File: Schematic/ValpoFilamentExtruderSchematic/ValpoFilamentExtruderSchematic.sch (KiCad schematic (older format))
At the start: 1 part

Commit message: Schematic Started
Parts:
- added A?: A000067, ARDUINO_A000067, symbol ArduinoMega2560:A000067
- added M? (x2): Motor_Servo, symbol Motor:Motor_Servo
- added M?: Fan_3pin, symbol Motor:Fan_3pin
- added R?: 10k, symbol Device:R
- added TH? (x2): JTypeThermocouple, symbol Sensor_Temperature:PT100
- added U?: HeatingElement, symbol FilamentRecycler09:HeatingElement
- added U?: 120ACV_24VDC, symbol FilamentRecycler09:120ACV_24VDC
- added U?: A1101ELHL, Package_TO_SOT_SMD:SOT-23, symbol Sensor_Magnetic:A1101ELHL
- added U?: 24V_5V, symbol FilamentRecycler09:24V_5V
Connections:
- new net: U?.2 (GND), U?.4 (-V)
- new net: R?.2, U?.2 (VOUT)
- new net +24V: U?.3 (+V), U?.3 (Vin)
- new net +5V: R?.1, U?.1 (VCC), U?.Vout (6)
- new net GND: U?.3 (GND)
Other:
- moved on the sheet: M?
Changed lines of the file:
@@
 L Motor:Motor_DC M?
 U 1 1 5F8662F0
-P 1750 1750
-F 0 "M?" H 1908 1746 50  0000 L CNN
-F 1 "Motor_DC" H 1908 1655 50  0000 L CNN
-F 2 "" H 1750 1660 50  0001 C CNN
-F 3 "~" H 1750 1660 50  0001 C CNN
-	1    1750 1750
-	1    0    0    -1
-$EndComp
+P 1250 2700
+F 0 "M?" H 1408 2696 50  0000 L CNN
+F 1 "Motor_DC" H 1408 2605 50  0000 L CNN
+F 2 "" H 1250 2610 50  0001 C CNN
+F 3 "~" H 1250 2610 50  0001 C CNN
+	1    1250 2700
+	1    0    0    -1
+$EndComp
+$Comp
+L ArduinoMega2560:A000067 A?
+U 1 1 5F887C03
+P 6850 3550
+F 0 "A?" H 6850 6117 50  0000 C CNN
+F 1 "A000067" H 6850 6026 50  0000 C CNN
+F 2 "ARDUINO_A000067" H 6850 3550 50  0001 L BNN
+F 3 "Unavailable" H 6850 3550 50  0001 L BNN
+F 4 "None" H 6850 3550 50  0001 L BNN "Field4"
+F 5 "Dev.kit: Arduino; SPI, TWI, UART; ICSP, USB B, pin strips, supply" H 6850 3550 50  0001 L BNN "Field5"
+F 6 "None" H 6850 3550 50  0001 L BNN "Field6"
+F 7 "ARDUINO MEGA2560 REV3 - RETAIL" H 6850 3550 50  0001 L BNN "Field7"
+F 8 "Arduino" H 6850 3550 50  0001 L BNN "Field8"
+	1    6850 3550
+	1    0    0    -1
+$EndComp
+$Comp
+L Sensor_Temperature:PT100 TH?
+U 1 1 5F890441
+P 2200 1600
+F 0 "TH?" H 2298 1646 50  0000 L CNN
+F 1 "JTypeThermocouple" H 2298 1555 50  0000 L CNN
+F 2 "" H 2200 1650 50  0001 C CNN
+F 3 "https://www.heraeus.com/media/media/group/doc_group/products_1/hst/sot_to/de_15/to_92_d.pdf" H 2200 1650 50  0001 C CNN
+	1    2200 1600
+	1    0    0    -1
+$EndComp
+$Comp
+L Sensor_Temperature:PT100 TH?
+U 1 1 5F891ED8
+P 1100 1600
+F 0 "TH?" H 1198 1646 50  0000 L CNN
+F 1 "JTypeThermocouple" H 1198 1555 50  0000 L CNN
+F 2 "" H 1100 1650 50  0001 C CNN
+F 3 "https://www.heraeus.com/media/media/group/doc_group/products_1/hst/sot_to/de_15/to_92_d.pdf" H 1100 1650 50  0001 C CNN
+	1    1100 1600
+	1    0    0    -1
+$EndComp
+$Comp
+L FilamentRecycler09:HeatingElement U?
+U 1 1 5F893064
+P 2800 900
+F 0 "U?" H 3042 1125 50  0000 C CNN
+F 1 "HeatingElement" H 3042 1034 50  0000 C CNN
+F 2 "" H 2800 1000 50  0001 C CNN
+F 3 "" H 2800 1000 50  0001 C CNN
+	1    2800 900
+	1    0    0    -1
+$EndComp
+$Comp
+L Motor:Motor_Servo M?
+U 1 1 5F8966D7
+P 4800 2100
+F 0 "M?" H 5132 2165 50  0000 L CNN
+F 1 "Motor_Servo" H 5132 2074 50  0000 L CNN
+F 2 "" H 4800 1910 50  0001 C CNN
+F 3 "http://forums.parallax.com/uploads/attachments/46831/74481.png" H 4800 1910 50  0001 C CNN
+	1    4800 2100
+	1    0    0    -1
+$EndComp
+$Comp
+L Motor:Motor_Servo M?
+U 1 1 5F88F163
+P 4800 2500
+F 0 "M?" H 5132 2565 50  0000 L CNN
+F 1 "Motor_Servo" H 5132 2474 50  0000 L CNN
+F 2 "" H 4800 2310 50  0001 C CNN
+F 3 "http://forums.parallax.com/uploads/attachments/46831/74481.png" H 4800 2310 50  0001 C CNN
+	1    4800 2500
+	1    0    0    -1
+$EndComp
+$Comp
+L FilamentRecycler09:120ACV_24VDC U?
+U 1 1 5F8A2677
+P 1650 4050
+F 0 "U?" H 1700 4615 50  0000 C CNN
+F 1 "120ACV_24VDC" H 1700 4524 50  0000 C CNN
+F 2 "" H 1650 4600 50  0001 C CNN
+F 3 "" H 1650 4600 50  0001 C CNN
+	1    1650 4050
+	1    0    0    -1
+$EndComp
+$Comp
+L FilamentRecycler09:24V_5V U?
+U 1 1 5F8A3A69
+P 3150 4000
+F 0 "U?" H 3175 4415 50  0000 C CNN
+F 1 "24V_5V" H 3175 4324 50  0000 C CNN
+F 2 "" H 3150 4250 50  0001 C CNN
+F 3 "" H 3150 4250 50  0001 C CNN
+	1    3150 4000
+	1    0    0    -1
+$EndComp
+Wire Wire Line
+	2100 3950 2150 3950
+Wire Wire Line
+	2500 3950 2500 4150
+Wire Wire Line
+	2500 4150 2850 4150
+Wire Wire Line
+	2850 4000 2250 4000
+Wire Wire Line
+	2250 4000 2250 4050
+Wire Wire Line
+	2250 4050 2100 4050
+$Comp
+L Motor:Fan_3pin M?
+U 1 1 5F8A2653
+P 4100 5100
+F 0 "M?" H 4258 5096 50  0000 L CNN
+F 1 "Fan_3pin" H 4258 5005 50  0000 L CNN
+F 2 "" H 4100 5010 50  0001 C CNN
+F 3 "http://www.hardwarecanucks.com/forum/attachments/new-builds/16287d1330775095-help-chassis-power-fan-connectors-motherboard-asus_p8z68.jpg" H 4100 5010 50  0001 C CNN
+	1    4100 5100
+	1    0    0    -1
+$EndComp
+$Comp
+L Sensor_Magnetic:A1101ELHL U?
+U 1 1 5F8A36D5
+P 1750 5400
+F 0 "U?" H 1520 5446 50  0000 R CNN
+F 1 "A1101ELHL" H 1520 5355 50  0000 R CNN
+F 2 "Package_TO_SOT_SMD:SOT-23" H 1750 5050 50  0001 L CIN
+F 3 "http://www.allegromicro.com/en/Products/Part_Numbers/1101/1101.pdf" H 1750 6050 50  0001 C CNN
+	1    1750 5400
+	1    0    0    -1
+$EndComp
+$Comp
+L Device:R R?
+U 1 1 5F8A3F4C
+P 2450 5400
+F 0 "R?" H 2520 5446 50  0000 L CNN
+F 1 "10k" H 2520 5355 50  0000 L CNN
+F 2 "" V 2380 5400 50  0001 C CNN
+F 3 "~" H 2450 5400 50  0001 C CNN
+	1    2450 5400
+	1    0    0    -1
+$EndComp
+Wire Wire Line
+	1650 5000 2000 5000
+Wire Wire Line
+	2450 5000 2450 5250
+Wire Wire Line
+	2450 5550 2050 5550
+Wire Wire Line
+	2050 5400 2050 5550
+$Comp
+L power:GND #PWR?
+U 1 1 5F8A4EB8
+P 1650 5800
+F 0 "#PWR?" H 1650 5550 50  0001 C CNN
+F 1 "GND" H 1655 5627 50  0000 C CNN
+F 2 "" H 1650 5800 50  0001 C CNN
+F 3 "" H 1650 5800 50  0001 C CNN
+	1    1650 5800
+	1    0    0    -1
+$EndComp
+Wire Wire Line
+	3500 4150 3900 4150
+$Comp
+L power:+5V #PWR?
+U 1 1 5F8A6013
+P 3900 4150
+F 0 "#PWR?" H 3900 4000 50  0001 C CNN
+F 1 "+5V" H 3915 4323 50  0000 C CNN
+F 2 "" H 3900 4150 50  0001 C CNN
+F 3 "" H 3900 4150 50  0001 C CNN
+	1    3900 4150
+	1    0    0    -1
+$EndComp
+$Comp
+L power:+24V #PWR?
+U 1 1 5F8A6838
+P 2150 3950
+F 0 "#PWR?" H 2150 3800 50  0001 C CNN
+F 1 "+24V" H 2165 4123 50  0000 C CNN
+F 2 "" H 2150 3950 50  0001 C CNN
+F 3 "" H 2150 3950 50  0001 C CNN
+	1    2150 3950
+	1    0    0    -1
+$EndComp
+Connection ~ 2150 3950
+Wire Wire Line
+	2150 3950 2500 3950
+$Comp
+L power:+5V #PWR?
+U 1 1 5F8A6C16
+P 2000 5000
+F 0 "#PWR?" H 2000 4850 50  0001 C CNN
+F 1 "+5V" H 2015 5173 50  0000 C CNN
+F 2 "" H 2000 5000 50  0001 C CNN
+F 3 "" H 2000 5000 50  0001 C CNN
+	1    2000 5000
+	1    0    0    -1
+$EndComp
+Connection ~ 2000 5000
+Wire Wire Line
+	2000 5000 2450 5000
 $EndSCHEMATC

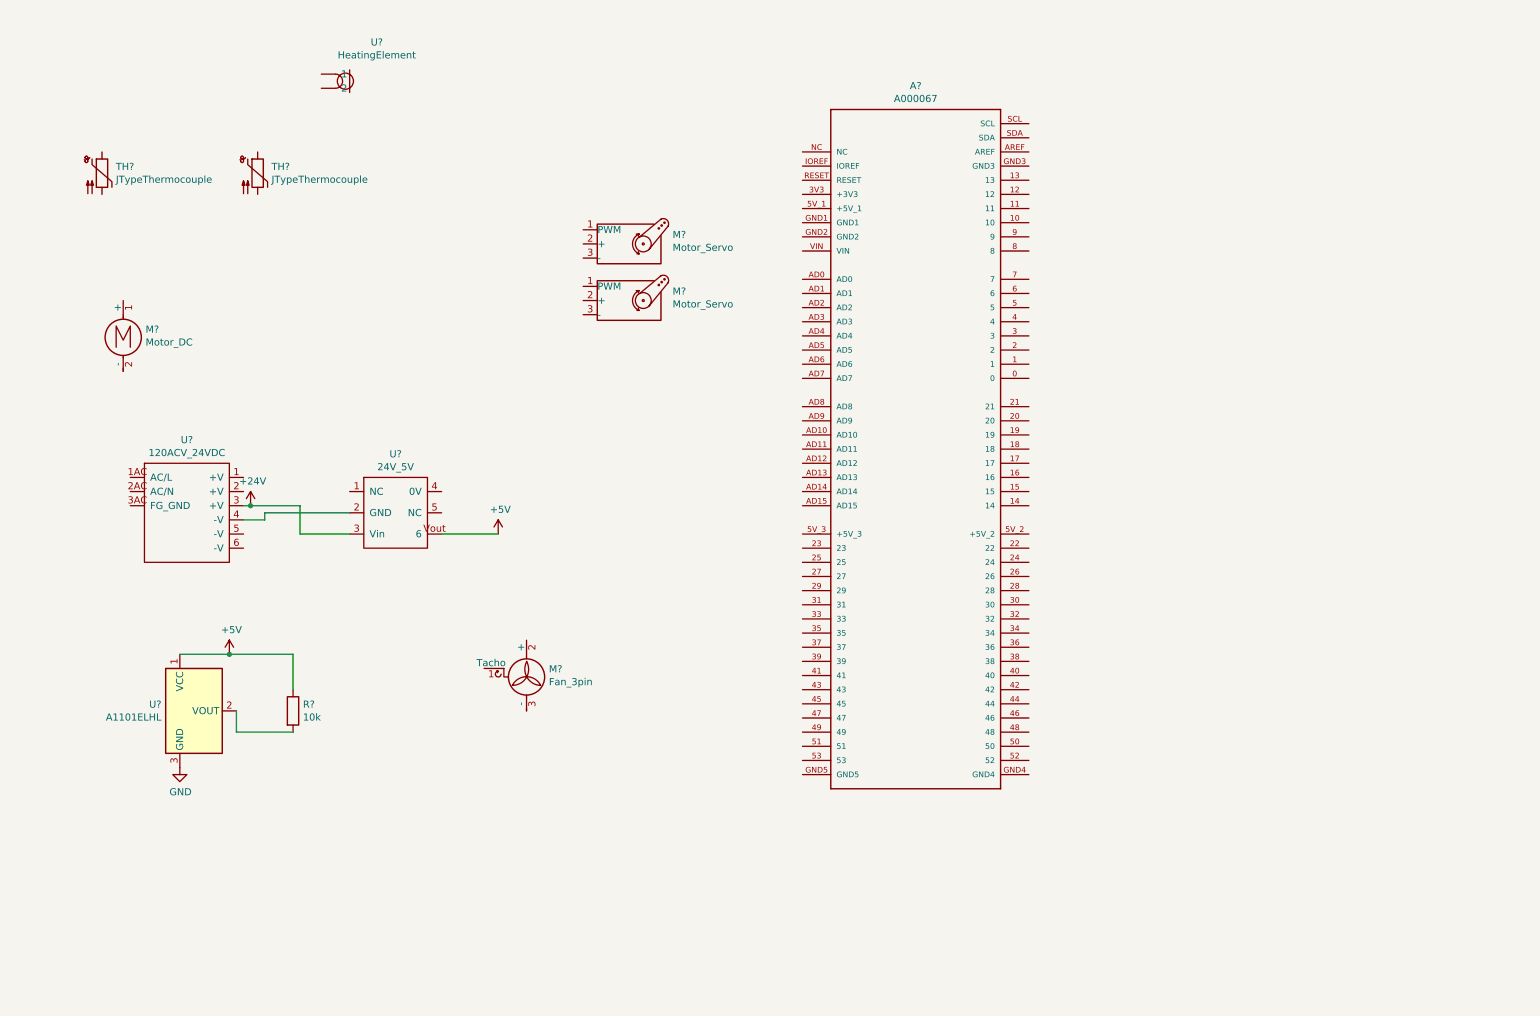
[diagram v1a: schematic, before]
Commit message: Added first version of schematic
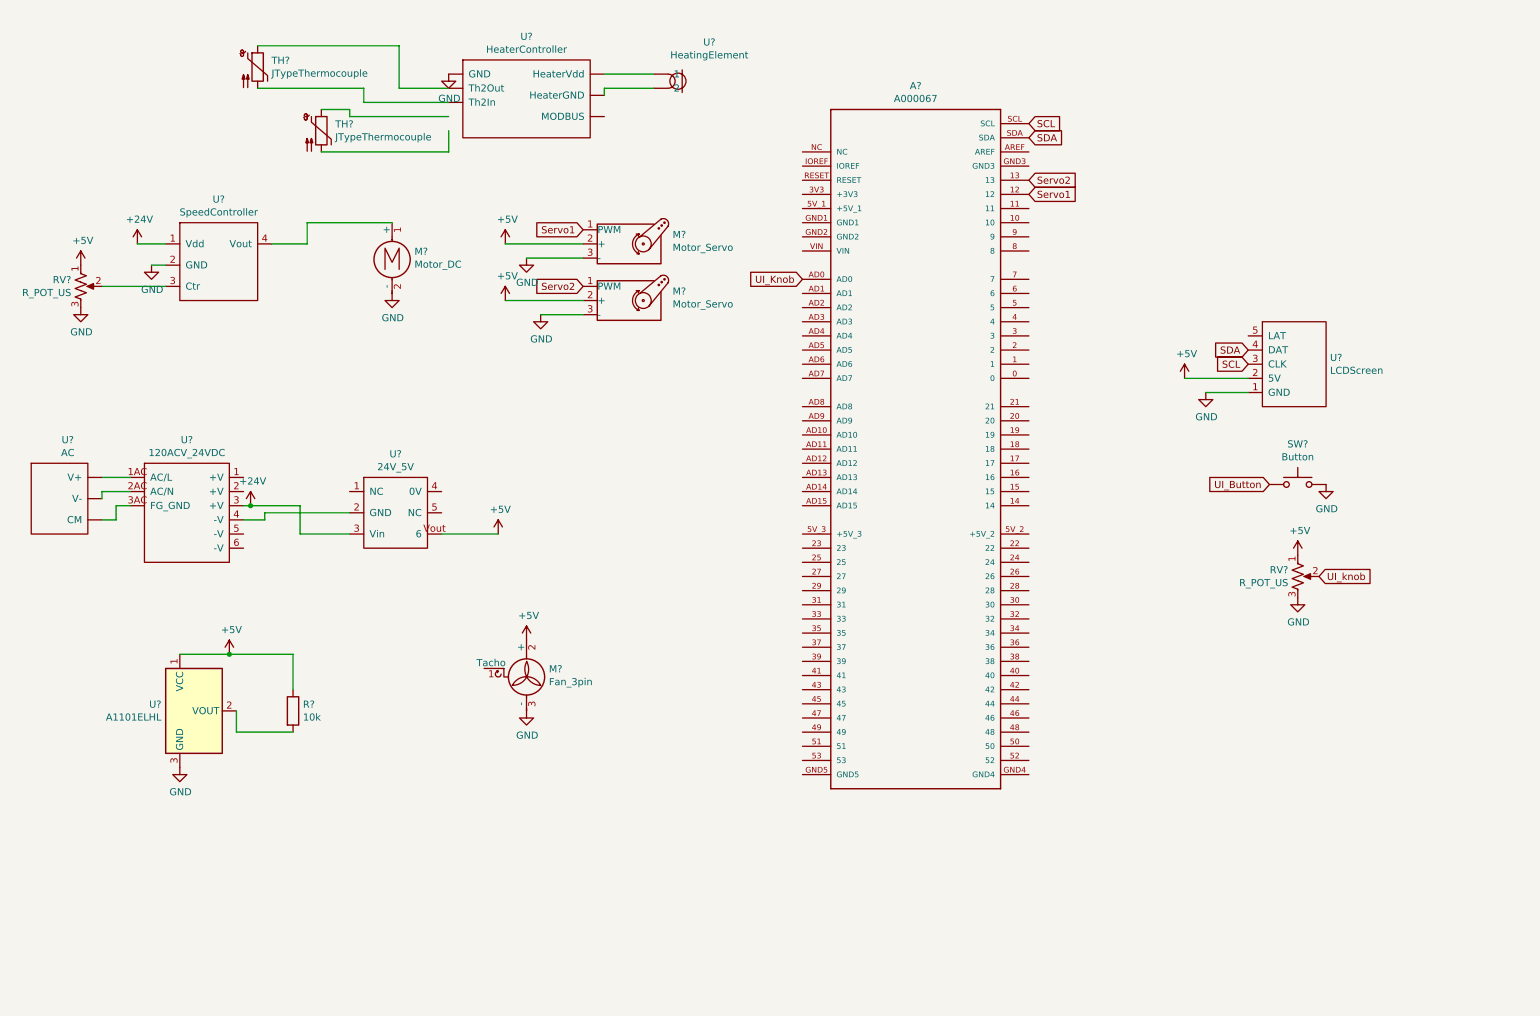
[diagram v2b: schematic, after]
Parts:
- added RV? (x2): R_POT_US, symbol Device:R_POT_US
- added SW?: Button, symbol Switch:SW_MEC_5G
- added U?: LCDScreen, symbol FilamentRecycler09:LCDScreen
- added U?: AC, symbol FilamentRecycler09:AC
- added U?: SpeedController, symbol FilamentRecycler09:SpeedController
- added U?: HeaterController, symbol FilamentRecycler09:HeaterController
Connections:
- net labels added: SCL, SDA, Servo1, Servo2, UI_Button, UI_Knob, UI_knob
- wire segments 13 -> 45
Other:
- moved on the sheet: M?, TH?, U?

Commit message: Added Stuff
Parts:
- removed RV?: R_POT_US, symbol Device:R_POT_US
- removed TH?: JTypeThermocouple, symbol Sensor_Temperature:PT100
- added K1: ADW11, Relay_THT:Relay_1P1T_NO_10x24x18.8mm_Panasonic_ADW11xxxxW_THT, symbol Relay:ADW11
- added R?: 100, symbol Device:R
- added R?: R, symbol Device:R
- added SW?: SW_Push, symbol Switch:SW_Push
- added U10: ARDUINO_MKR_485_SHIELD, symbol FilamentRecycler09:ARDUINO_MKR_485_SHIELD
- added U9: MCP4725_Breakout_Board, symbol FilamentRecycler09:MCP4725_Breakout_Board
- added U?: T_Slot_Photo_Interrupter, symbol FilamentRecycler09:T_Slot_Photo_Interrupter
- gave numbers to parts that had none: 17
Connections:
- net labels added: CM, HAL, Photo1, RX, TX, V+
- wire segments 45 -> 59
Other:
- moved on the sheet: M1, M2, M3, M4, R1, TH1, U1, U2, U3, U4, U5, U6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

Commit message: Updates
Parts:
- removed SW?: SW_Push, symbol Switch:SW_Push
- added Q1: 2N7000, Package_TO_SOT_THT:TO-92_Inline, symbol Transistor_FET:2N7000
- added R4: 100, symbol Device:R
- added R5: R, symbol Device:R
- added U12: LoadCell, symbol FilamentRecycler09:LoadCell
- added U13: T_Slot_Photo_Interrupter, symbol FilamentRecycler09:T_Slot_Photo_Interrupter
- gave numbers to parts that had none: 3
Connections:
- net +24V: now also U5.3 (Vin)
- net +5V: now also Q1.3 (D), R4.1, U12.~ (Vcc), U13.~ (Vin); no longer M2.2 (+)
- net GND: now also R5.2, U12.~ (Vcc), U13.~ (Vin)
- net LOAD_SCK: now reaches A1.10
- net LOAD_SCK: now also U12.~ (Vcc)
- net LOAD_DT: now reaches A1.11
- net LOAD_DT: now also U12.~ (Vcc)
- net FAN_IO: now reaches A1.9
- net FAN_IO: now also Q1.2 (G)
- net Photo2: now reaches A1.AD3
- net Photo2: now also R5.1, U13.~ (Vin)
- new net: M2.2 (+), Q1.1 (S)
- new net: U10.~ (TX), U6.~ (Th2Out)
- new net: R4.2, U13.~ (Vin)
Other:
- moved on the sheet: M2, M3, M4, R2, R3, RV2, SW1, U11, U8
